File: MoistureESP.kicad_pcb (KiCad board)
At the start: 2 copper layers, 30.5 x 99.7 mm, 108 parts, among them J1 Conn_01x02_Pin, J2 Conn_MoisturePCB, J3 Conn_DS18B20, J4 Conn_01x06_Pin, J5 Conn_01x03_Pin, J6 Conn_01x04_Pin, J7 USB4110-GF-A, Q1 SSM6K513NU-LF, Q10 SI7137DP-T1-GE3, Q2 SSM6K513NU-LF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

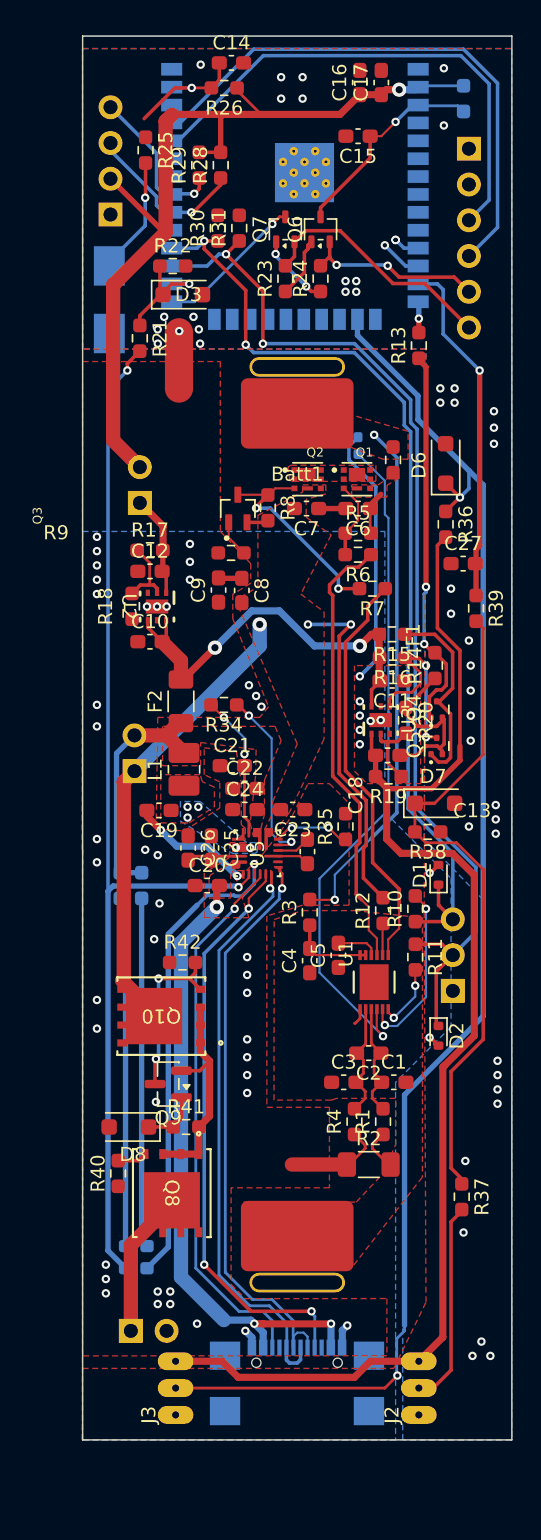
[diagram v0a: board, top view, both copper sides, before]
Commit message: Editing layout, redrawing analog and RTS DTS signals. Placing the silk layer designators
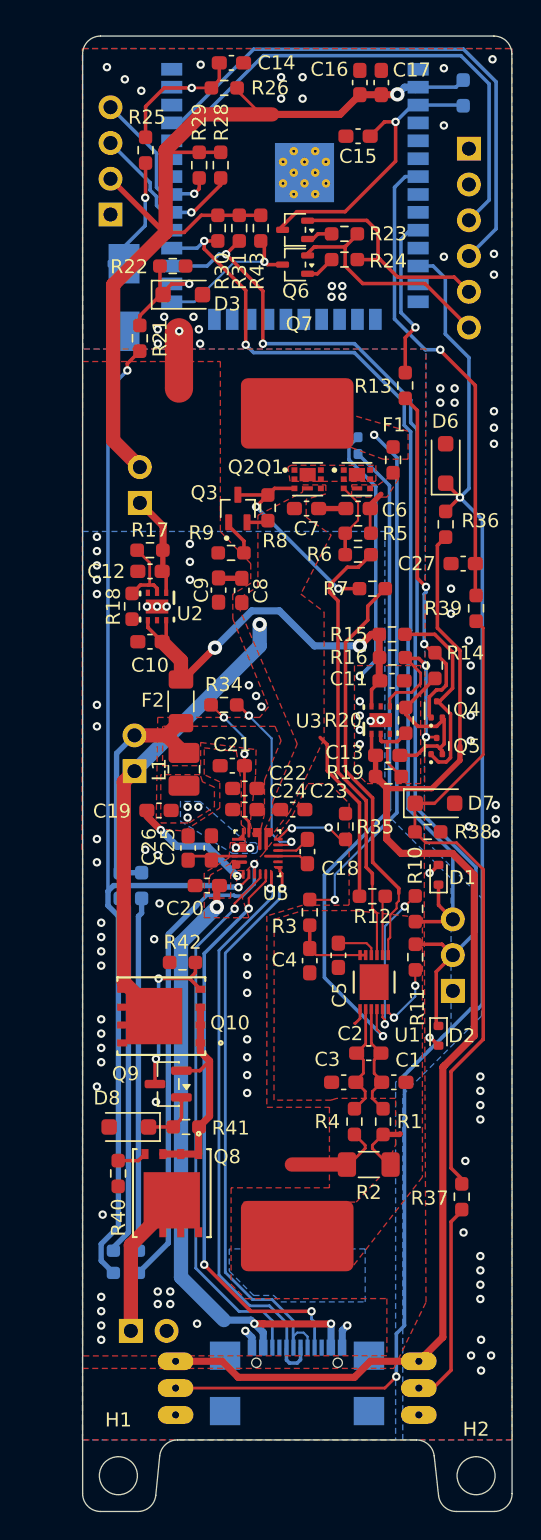
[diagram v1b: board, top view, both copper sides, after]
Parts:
- added H1: MountingHole, MountingHole:MountingHole_2.7mm_M2.5_DIN965, F.Cu at (38.1, 154.9)
- added H2: MountingHole, MountingHole:MountingHole_2.7mm_M2.5_DIN965, F.Cu at (63.5, 154.9)
- added R43: 10K, Resistor_SMD:R_0603_1608Metric_Pad0.98x0.95mm_HandSolder, F.Cu at (48.2, 66.3)
- moved R23 5.26 mm to (54.2, 66.8), turned to 0 degrees
- moved R13 3.00 mm to (58.5, 77.5)
- moved Q7 2.60 mm to (50.6, 68.9), turned to 180 degrees
- moved R24 2.17 mm to (54.2, 68.6), turned to 0 degrees
- moved Q6 1.81 mm to (50.6, 66.5), turned to 180 degrees
- moved R12 1.27 mm to (56.1, 113.8), turned to 180 degrees
- moved SW1 1.06 mm to (38.5, 71.3)
- moved D5 0.92 mm to (37.7, 139.8)
- moved D4 0.69 mm to (39.5, 139.8)
- moved R27 0.41 mm to (62.6, 56.7)
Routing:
- net VDD: track 61.6 -> 73.0 mm
- net /charger/VBat: track 58.3 -> 47.1 mm, vias 3 -> 1
- net /mcu/analog_enable: track 2.21 -> 11.7 mm
- net /mcu/analog_pin: track 24.9 -> 34.2 mm
- net Net-(Q6-C): track 14.9 -> 20.7 mm
- net /mcu/MCU.RTS: track 13.0 -> 16.7 mm, vias 2 -> 0
- net Net-(Q7-B): track 5.25 -> 2.12 mm, vias 2 -> 0
- net Net-(Q4-G): track 27.3 -> 24.8 mm
- net Net-(U1-PACK): track 2.26 -> 4.26 mm
- net unconnected-(U4-IO26-Pad11): track 1.86 -> 0.00 mm, vias 2 -> 0
- net Net-(Q6-B): track 4.29 -> 2.53 mm
- net /mcu/~{force_wakeup_prot}: track 9.13 -> 10.9 mm
- net /mcu/onewire_pin: track 105.4 -> 103.7 mm, vias 3 -> 2
- net /mcu/MCU.DTR: track 17.5 -> 16.3 mm
- net CGND: track 4.28 -> 5.52 mm
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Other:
- board size 30.5 x 99.7 mm -> 30.5 x 104.8 mm
- board text added: "INOK"

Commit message: Modify zones and adjustmenents in analog power.
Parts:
- moved D2 1.41 mm to (60.3, 122.4)
- moved Q5 0.45 mm to (61.0, 102.8), turned to -90 degrees
- moved Q4 0.43 mm to (61.1, 100.4), turned to 0 degrees
- moved R18 0.31 mm to (38.8, 93.2)
- moved R20 0.26 mm to (58.8, 101.3)
- moved C9 0.23 mm to (45.0, 92.0)
- moved C26 0.10 mm to (43.0, 110.4)
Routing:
- net Net-(Q4-D): track 14.2 -> 9.99 mm
- net GNDPWR: track 44.0 -> 41.5 mm, vias 60 -> 66
- net Net-(Q9-E): track 15.9 -> 18.1 mm
- net /battery/comm.SDA: track 76.0 -> 74.4 mm
- net Net-(Q4-G): track 24.8 -> 23.5 mm
- net Net-(Q5-D): track 13.1 -> 14.3 mm
- net /charger/CC2: track 38.8 -> 37.9 mm
- net VBUS: track 44.6 -> 43.7 mm

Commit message: Edit silkscreen.
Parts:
- moved R26 4.30 mm to (41.5, 57.5), turned to 90 degrees
- moved C14 1.88 mm to (45.5, 56.4)
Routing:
- net /mcu/~{force_wakeup_prot}: track 10.9 -> 8.67 mm
- net CGND: track 5.52 -> 4.28 mm
- net /mcu/analog_pin: track 34.2 -> 33.5 mm
- net GNDPWR: vias 66 -> 71
- net GNDD: vias 57 -> 71
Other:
- board text added: "1W"
- board text added: "C"
- board text added: "CHGR"
- board text added: "D"
- board text added: "DTR"
- board text added: "GND"
- board text added: "GNDD"
- board text added: "MoistureESP V1.0"
- board text added: "RTS"
- board text added: "Rx"
- board text added: "SCL"
- board text added: "SDA"
- board text added: "Tx"
- board text added: "VDD"
- board text added: "Van"
- board text added: "Vbus"
- board text added: "Vmoist"

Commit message: Delete temporary files.
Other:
- board text added: "+"
- board text added: "-"
- board text added: "VMCU"
- board text added: "Vbat"
- board text added: "Vsys"

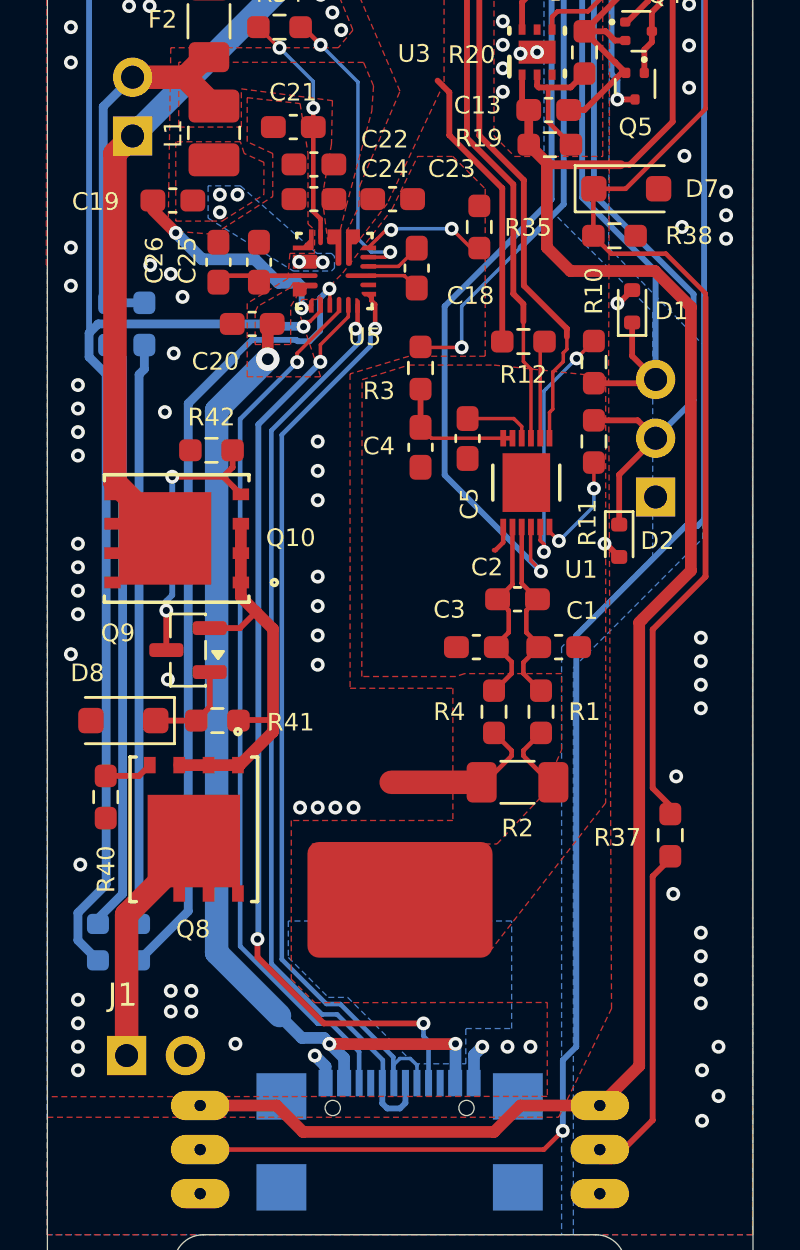
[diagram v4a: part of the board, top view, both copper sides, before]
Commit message: Editing silkscreen, move battery charge connector.
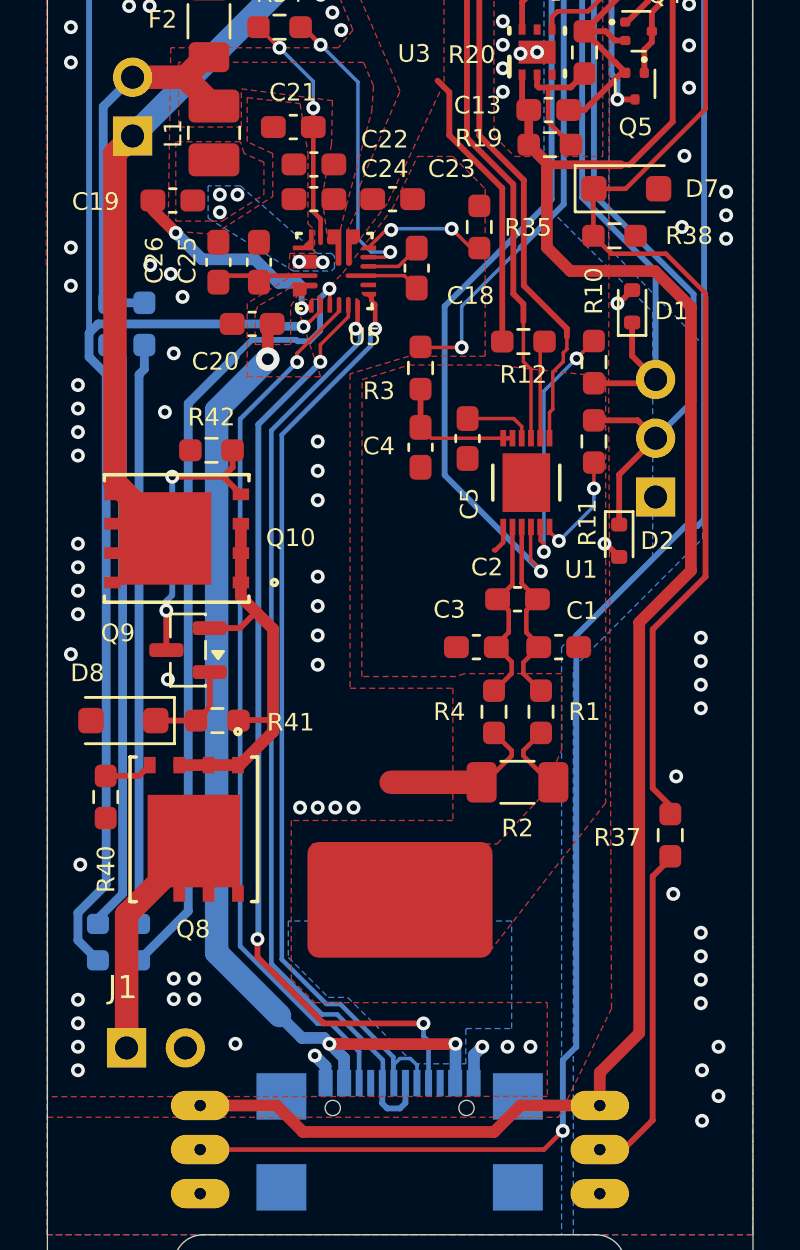
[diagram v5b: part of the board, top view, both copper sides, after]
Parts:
- moved J1 0.33 mm to (39.0, 144.3)
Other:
- board text added: "Designed for Li-Ion battery."
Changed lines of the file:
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@@
 		(capping no)
 		(filling no)
+		(zone_defaults)
 		(pcbplotparams
 			(layerselection 0x00000000_00000000_55555555_5755f5ff)
@@
 		(tags "Through hole pin header THT 1x04 2.54mm single row")
 		(property "Reference" "J6"
-			(at -0.254 -9.8552 -0)
+			(at -0.254 -9.8552 0)
 			(layer "F.SilkS")
 			(effects
@@
 		(tags "Through hole pin header THT 1x06 2.54mm single row")
 		(property "Reference" "J4"
-			(at -1.27 2.3876 -0)
+			(at -1.27 2.3876 0)
 			(layer "F.SilkS")
 			(effects
@@
 		(tags "Through hole pin header THT 1x02 2.54mm single row")
 		(property "Reference" "JP2"
-			(at 0 -5.085 -0)
+			(at 0 -5.085 0)
 			(layer "F.SilkS")
 			(effects
@@
 	(footprint "Connector_PinHeader_2.54mm:PinHeader_1x02_P2.54mm_Vertical"
 		(layer "B.Cu")
-		(at 38.984 144.653 -90)
+		(at 38.984 144.3228 -90)
 		(descr "Through hole straight pin header, 1x02, 2.54mm pitch, single row")
 		(tags "Through hole pin header THT 1x02 2.54mm single row")
 		(property "Reference" "J1"
-			(at -2.6162 0.1728 -180)
+			(at -2.6162 0.1728 180)
 			(layer "F.SilkS")
 			(effects
@@
 		)
 	)
+	(gr_text "Designed for Li-Ion battery."
+		(at 44.5008 76.8096 90)
+		(layer "B.SilkS" knockout)
+		(effects
+			(font
+				(size 0.762 0.762)
+				(thickness 0.1524)
+				(italic yes)
+			)
+			(justify left bottom mirror)
+		)
+	)
 	(gr_text "+"
-		(at 39.6748 142.9512 0)
+		(at 39.7256 142.748 0)
 		(layer "B.SilkS" knockout)
 		(effects
@@
 	)
 	(via
-		(at 41.783 141.859)
+		(at 41.91 141.3256)
 		(size 0.6)
 		(drill 0.3)
@@
 	)
 	(via
-		(at 40.894 141.859)
+		(at 41.021 141.3256)
 		(size 0.6)
 		(drill 0.3)
@@
 	)
 	(via
-		(at 40.894 142.748)
+		(at 41.021 142.2146)
 		(size 0.6)
 		(drill 0.3)
@@
 	)
 	(via
-		(at 41.783 142.748)
+		(at 41.91 142.2146)
 		(size 0.6)
 		(drill 0.3)
@@
 	)
 	(segment
-		(start 41.764001 135.781999)
-		(end 38.984 138.562)
+		(start 41.764001 135.255)
+		(end 41.764001 135.781999)
 		(width 1.016)
 		(layer "F.Cu")
@@
 	)
 	(segment
-		(start 38.984 138.562)
-		(end 38.984 144.653)
+		(start 41.764001 135.781999)
+		(end 38.984 138.562)
 		(width 1.016)
 		(layer "F.Cu")
@@
 	)
 	(segment
-		(start 41.764001 135.255)
-		(end 41.764001 135.781999)
+		(start 38.984 138.562)
+		(end 38.984 144.3228)
 		(width 1.016)
 		(layer "F.Cu")
@@
 	)
 	(segment
-		(start 61.141 145.107)
-		(end 59.436 146.812)
-		(width 0.508)
-		(layer "F.Cu")
-		(net "Van")
-	)
-	(segment
-		(start 61.141 125.93)
-		(end 61.141 145.107)
+		(start 58.166 110.744)
+		(end 61.81928 110.744)
 		(width 0.508)
 		(layer "F.Cu")
@@
 	)
 	(segment
-		(start 58.166 110.744)
-		(end 57.15 109.728)
-		(width 0.508)
-		(layer "F.Cu")
-		(net "Van")
-	)
-	(segment
-		(start 57.15 106.0685)
-		(end 56.3645 105.283)
+		(start 63.373 123.698)
+		(end 61.141 125.93)
 		(width 0.508)
 		(layer "F.Cu")
@@
 	)
 	(segment
-		(start 63.373 123.698)
-		(end 63.373 112.29772)
-		(width 0.508)
-		(layer "F.Cu")
-		(net "Van")
-	)
-	(segment
 		(start 60.752955 94.735998)
 		(end 62.5856 96.568643)
@@
 	)
 	(segment
-		(start 61.2775 125.7935)
-		(end 63.373 123.698)
+		(start 59.436 145.3896)
+		(end 59.436 146.812)
+		(width 0.508)
+		(layer "F.Cu")
+		(net "Van")
+	)
+	(segment
+		(start 61.141 125.93)
+		(end 61.141 143.6846)
 		(width 0.508)
 		(layer "F.Cu")
@@
 	)
 	(segment
-		(start 57.15 109.728)
-		(end 57.15 106.0685)
-		(width 0.508)
-		(layer "F.Cu")
-		(net "Van")
-	)
-	(segment
 		(start 56.3645 105.283)
 		(end 56.364501 103.783)
@@
 	)
 	(segment
-		(start 61.81928 110.744)
+		(start 56.3645 105.283)
+		(end 57.15 106.0685)
+		(width 0.508)
+		(layer "F.Cu")
+		(net "Van")
+	)
+	(segment
+		(start 61.141 143.6846)
+		(end 59.436 145.3896)
+		(width 0.508)
+		(layer "F.Cu")
+		(net "Van")
+	)
+	(segment
+		(start 63.373 112.29772)
+		(end 63.373 123.698)
+		(width 0.508)
+		(layer "F.Cu")
+		(net "Van")
+	)
+	(segment
+		(start 57.15 109.728)
 		(end 58.166 110.744)
 		(width 0.508)
@@
 	)
 	(segment
-		(start 61.2775 125.7935)
-		(end 61.141 125.93)
+		(start 57.15 106.0685)
+		(end 57.15 109.728)
 		(width 0.508)
 		(layer "F.Cu")
@@
 	)
 	(segment
-		(start 63.373 112.29772)
-		(end 61.81928 110.744)
+		(start 61.81928 110.744)
+		(end 63.373 112.29772)
 		(width 0.508)
 		(layer "F.Cu")

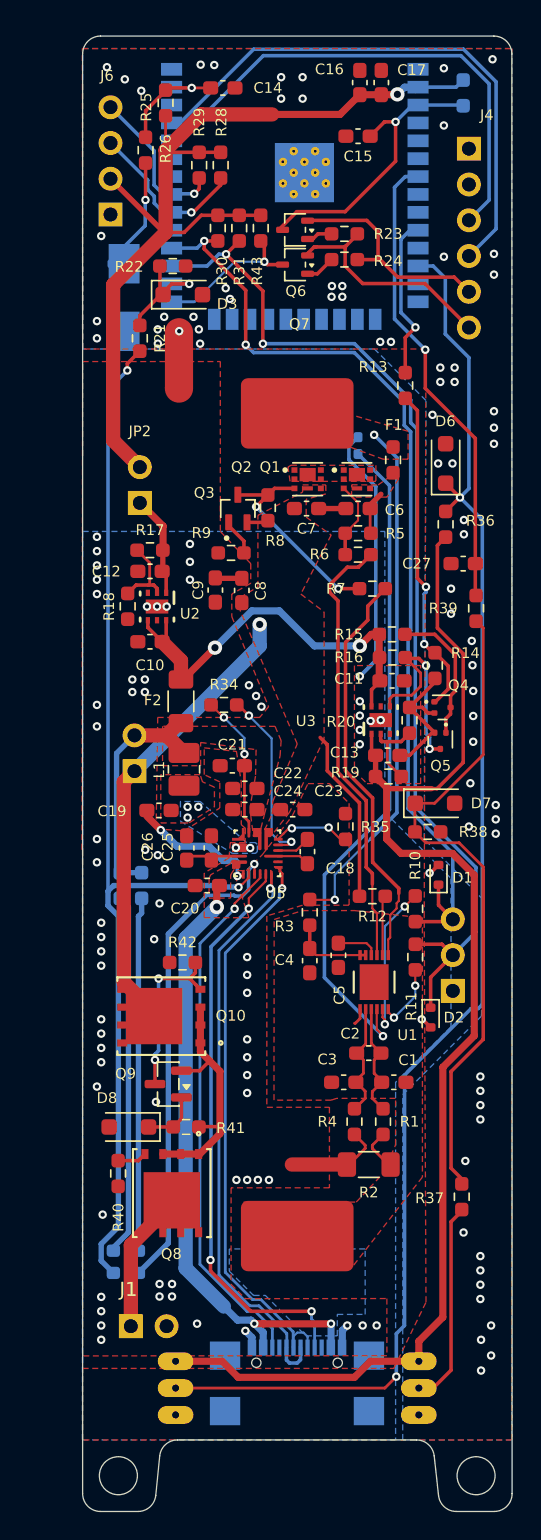
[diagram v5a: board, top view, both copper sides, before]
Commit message: Layout modification, refine connections and zone shapes.
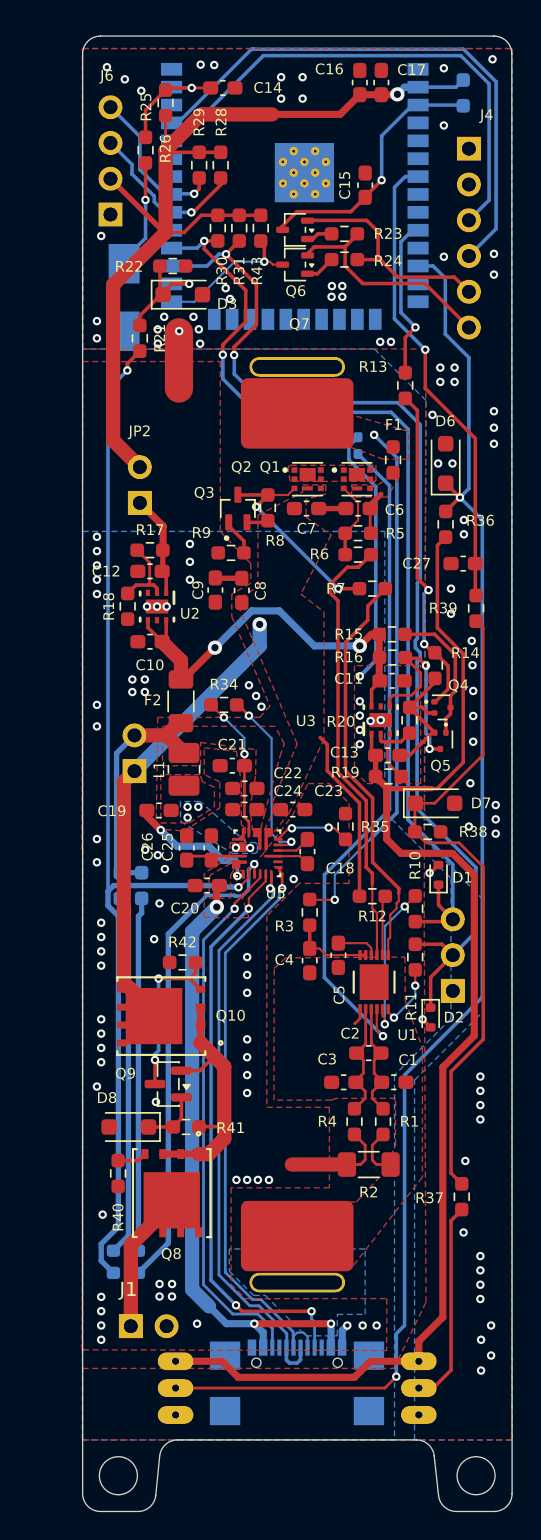
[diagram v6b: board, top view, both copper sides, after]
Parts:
- moved C15 3.52 mm to (55.6, 63.3), turned to 90 degrees
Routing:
- net /battery/comm.SDA: track 74.4 -> 77.9 mm
- net /battery/comm.SCL: track 68.9 -> 71.5 mm
- net Net-(Q6-C): track 20.7 -> 18.7 mm
- net GNDPWR: track 41.5 -> 40.6 mm
- net Net-(Q9-E): track 18.1 -> 18.8 mm
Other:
- board text added: "Designed for Li-Ion batteries."
- board text added: "Insulator"
- board text removed: "Designed for Li-Ion battery."

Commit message: Finish refinements, prepare to release.
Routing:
- net GNDPWR: track 40.6 -> 45.4 mm
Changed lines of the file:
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@@
 		(filling no)
 		(pcbplotparams
-			(layerselection 0x00000000_00000000_55555555_5755f5ff)
+			(layerselection 0x00000000_00000000_55555555_575555ff)
 			(plot_on_all_layers_selection 0x00000000_00000000_00000000_00000000)
 			(disableapertmacros no)
@@
 			(outputformat 1)
 			(mirror no)
-			(drillshape 1)
+			(drillshape 0)
 			(scaleselection 1)
 			(outputdirectory "")
@@
 			(drill oval 6.4 1)
 			(property pad_prop_mechanical)
-			(layers "*.Cu" "*.Mask")
+			(layers "*.Mask")
 			(remove_unused_layers no)
 			(clearance 0.1524)
@@
 			(size 6.8 1.4)
 			(drill oval 6.4 1)
-			(layers "*.Cu" "*.Mask")
+			(layers "*.Mask")
 			(remove_unused_layers no)
 			(solder_mask_margin 0)
@@
 	)
 	(segment
+		(start 47.584488 145.843279)
+		(end 47.584488 145.577688)
+		(width 0.381)
+		(layer "B.Cu")
+		(net "GNDPWR")
+	)
+	(segment
 		(start 54.000001 144.627999)
 		(end 54.356 144.272)
@@
 	)
 	(segment
+		(start 46.9392 144.9324)
+		(end 44.4754 144.9324)
+		(width 0.381)
+		(layer "B.Cu")
+		(net "GNDPWR")
+	)
+	(segment
 		(start 55.245 98.171)
 		(end 56.3795 97.0365)
@@
 	)
 	(segment
+		(start 44.4754 144.9324)
+		(end 43.688 144.145)
+		(width 0.381)
+		(layer "B.Cu")
+		(net "GNDPWR")
+	)
+	(segment
 		(start 54.471 81.8375)
 		(end 55.118 81.1905)
@@
 		(layer "B.Cu")
 		(net "GNDPWR")
+	)
+	(segment
+		(start 47.584488 145.577688)
+		(end 46.9392 144.9324)
+		(width 0.381)
+		(layer "B.Cu")
+		(net "GNDPWR")
